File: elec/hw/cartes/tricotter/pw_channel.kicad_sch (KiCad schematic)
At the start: 13 parts, among them J8 3-794618-4, Q11 G120P06M, Q12 2N7002

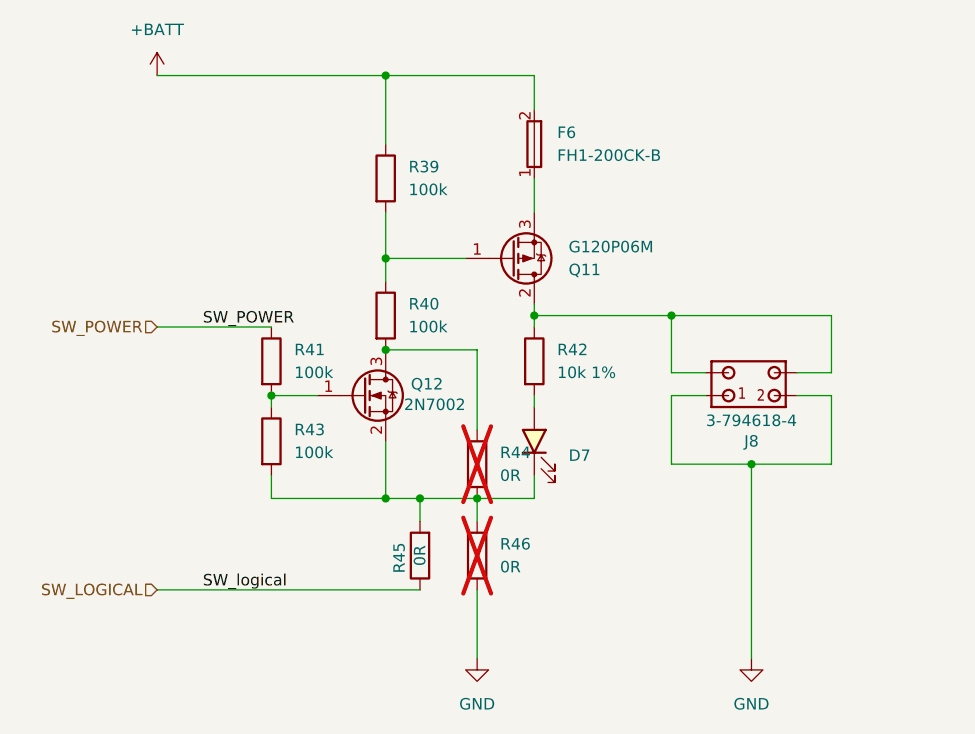
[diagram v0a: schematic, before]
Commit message: tricotter : reduced from 5 to 3 power channel and added chaining connector
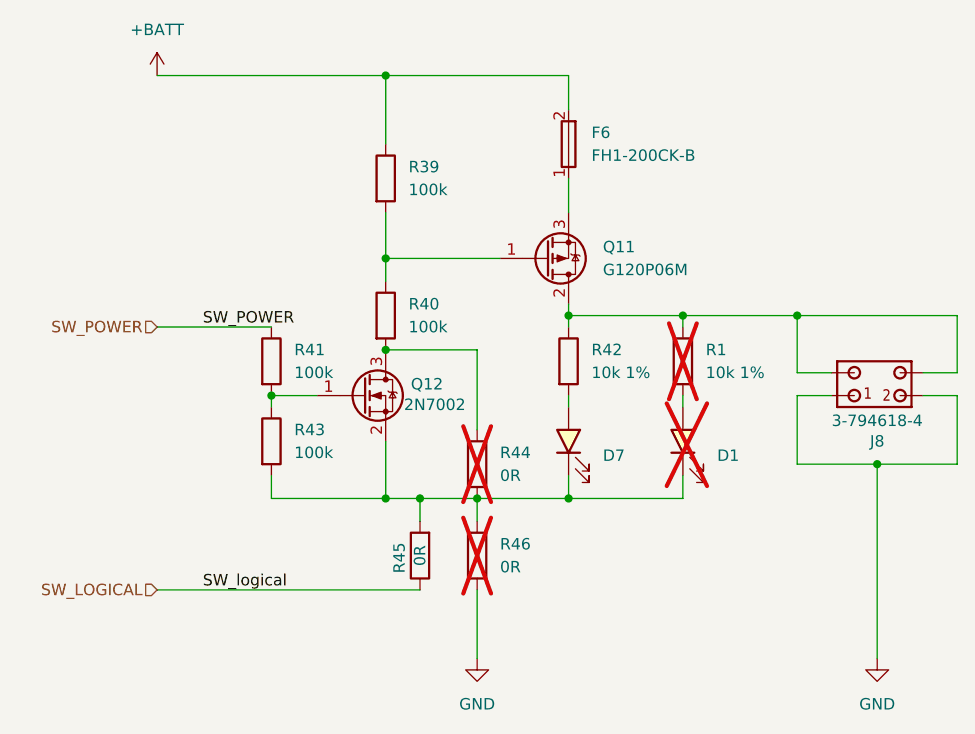
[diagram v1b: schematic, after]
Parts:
- added D1: green, 0603, cocotter_diodes:LED_0603_1608Metric, symbol cocotter_diodes:green_led_0603
- added R1: 10k 1%, cocotter_resistor:r0603_reflow, symbol cocotter_resistors:R_10k_0603_1%
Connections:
- net at J8.3, J8.4, Q11.2 (D)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: now also R1.1
- net at D7.C, Q12.2 (S), R43.2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: now also D1.C
- new net: D1.A, R1.2
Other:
- moved on the sheet: D7, F6, J8, Q11, R42

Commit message: tricotter 2027 schematic
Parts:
- R1, R39, R40, R41, R42, R43: mouser 603-RC0603FR-10100KL -> (none)
